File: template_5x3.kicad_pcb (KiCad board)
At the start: 2 copper layers, 120.7 x 66 mm, 1 part

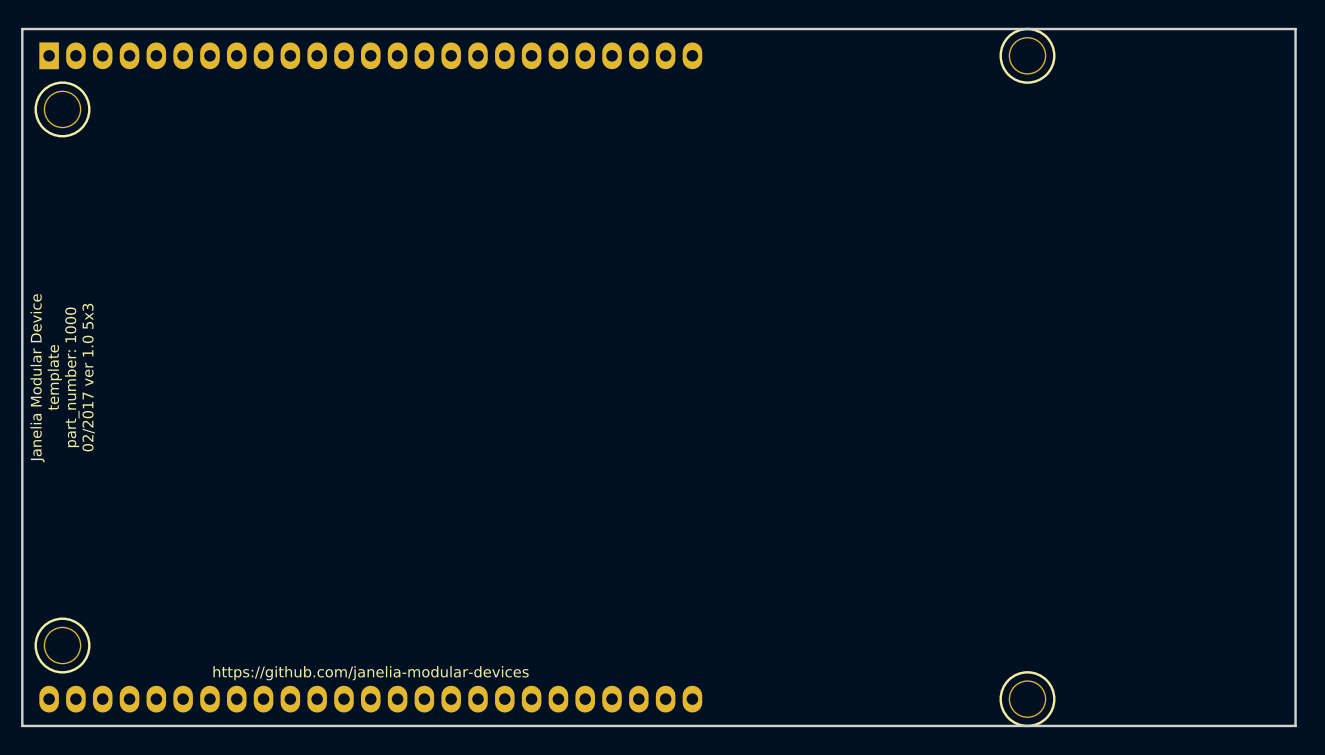
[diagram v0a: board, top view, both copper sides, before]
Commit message: Moved edge positions.
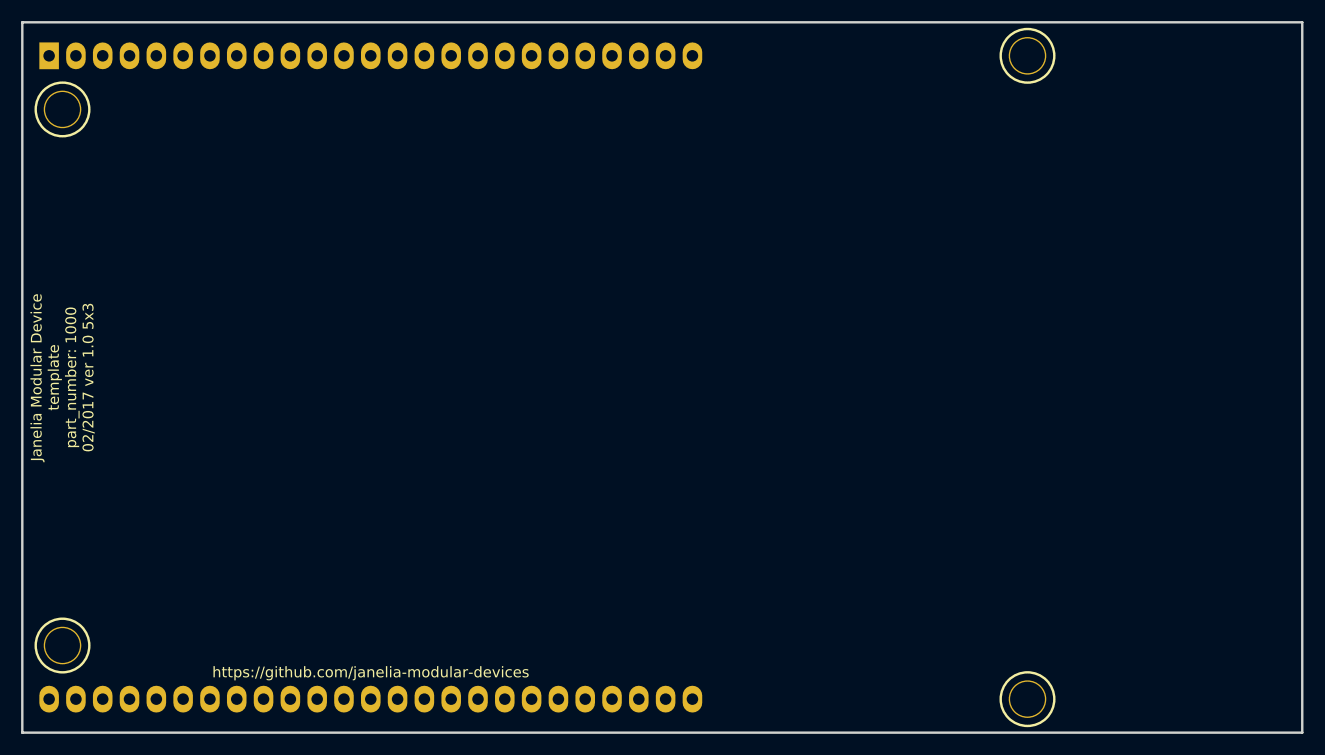
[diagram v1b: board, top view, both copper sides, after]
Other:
- board size 120.7 x 66 mm -> 121.3 x 67.3 mm
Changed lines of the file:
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@@
-(kicad_pcb (version 20170123) (host pcbnew no-vcs-found-ea855c1~58~ubuntu16.04.1)
+(kicad_pcb (version 20170123) (host pcbnew no-vcs-found-0633d90~59~ubuntu16.04.1)
   (general
-    (links 0)
-    (no_connects 0)
-    (area 69.481699 72.021699 190.868301 138.798301)
     (thickness 1.6)
     (drawings 6)
@@
     (47 F.CrtYd user)
     (48 B.Fab user)
-    (49 F.Fab user)
+    (49 F.Fab user hide)
   )
   (setup
@@
     (fp_line (start -20.32 31.75) (end 43.18 31.75) (layer B.SilkS) (width 0.381))
     (fp_line (start -20.32 29.21) (end 43.18 29.21) (layer B.SilkS) (width 0.381))
-    (fp_line (start 99.06 -33.02) (end -21.59 -33.02) (layer F.Fab) (width 0.2286))
-    (fp_line (start 99.06 33.02) (end 99.06 -33.02) (layer F.Fab) (width 0.2286))
-    (fp_line (start -21.59 33.02) (end 99.06 33.02) (layer F.Fab) (width 0.2286))
-    (fp_line (start -21.59 -33.02) (end -21.59 33.02) (layer F.Fab) (width 0.2286))
+    (fp_line (start 99.695 -33.655) (end -21.59 -33.655) (layer F.Fab) (width 0.2286))
+    (fp_line (start 99.695 33.655) (end 99.695 -33.655) (layer F.Fab) (width 0.2286))
+    (fp_line (start -21.59 33.655) (end 99.695 33.655) (layer F.Fab) (width 0.2286))
+    (fp_line (start -21.59 -33.655) (end -21.59 33.655) (layer F.Fab) (width 0.2286))
     (fp_line (start 43.18 -29.21) (end 43.18 -31.75) (layer B.SilkS) (width 0.381))
     (fp_line (start -20.32 -31.75) (end -20.32 -29.21) (layer B.SilkS) (width 0.381))
@@
     (pad GND thru_hole oval (at -16.51 -30.48) (size 1.8542 2.54) (drill 1.0922) (layers *.Cu *.Mask))
   )
-  (gr_line (start 190.5 72.39) (end 69.85 72.39) (angle 90) (layer Edge.Cuts) (width 0.2286))
-  (gr_line (start 190.5 138.43) (end 190.5 72.39) (angle 90) (layer Edge.Cuts) (width 0.2286))
-  (gr_line (start 69.85 138.43) (end 190.5 138.43) (angle 90) (layer Edge.Cuts) (width 0.2286))
-  (gr_line (start 69.85 72.39) (end 69.85 138.43) (angle 90) (layer Edge.Cuts) (width 0.2286))
+  (gr_line (start 191.135 71.755) (end 69.85 71.755) (angle 90) (layer Edge.Cuts) (width 0.2286))
+  (gr_line (start 191.135 139.065) (end 191.135 71.755) (angle 90) (layer Edge.Cuts) (width 0.2286))
+  (gr_line (start 69.85 139.065) (end 191.135 139.065) (angle 90) (layer Edge.Cuts) (width 0.2286))
+  (gr_line (start 69.85 71.755) (end 69.85 139.065) (angle 90) (layer Edge.Cuts) (width 0.2286))
   (gr_text https://github.com/janelia-modular-devices (at 102.87 133.35) (layer F.SilkS)
     (effects (font (size 1.016 1.016) (thickness 0.1905)))
